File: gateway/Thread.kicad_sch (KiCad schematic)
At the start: 27 parts, among them IC1004 MIC5317-3.3xM5, IC1501 TXB0104PWR, M1501 BT40, Q1501 BSS123, X1501 DEBUG

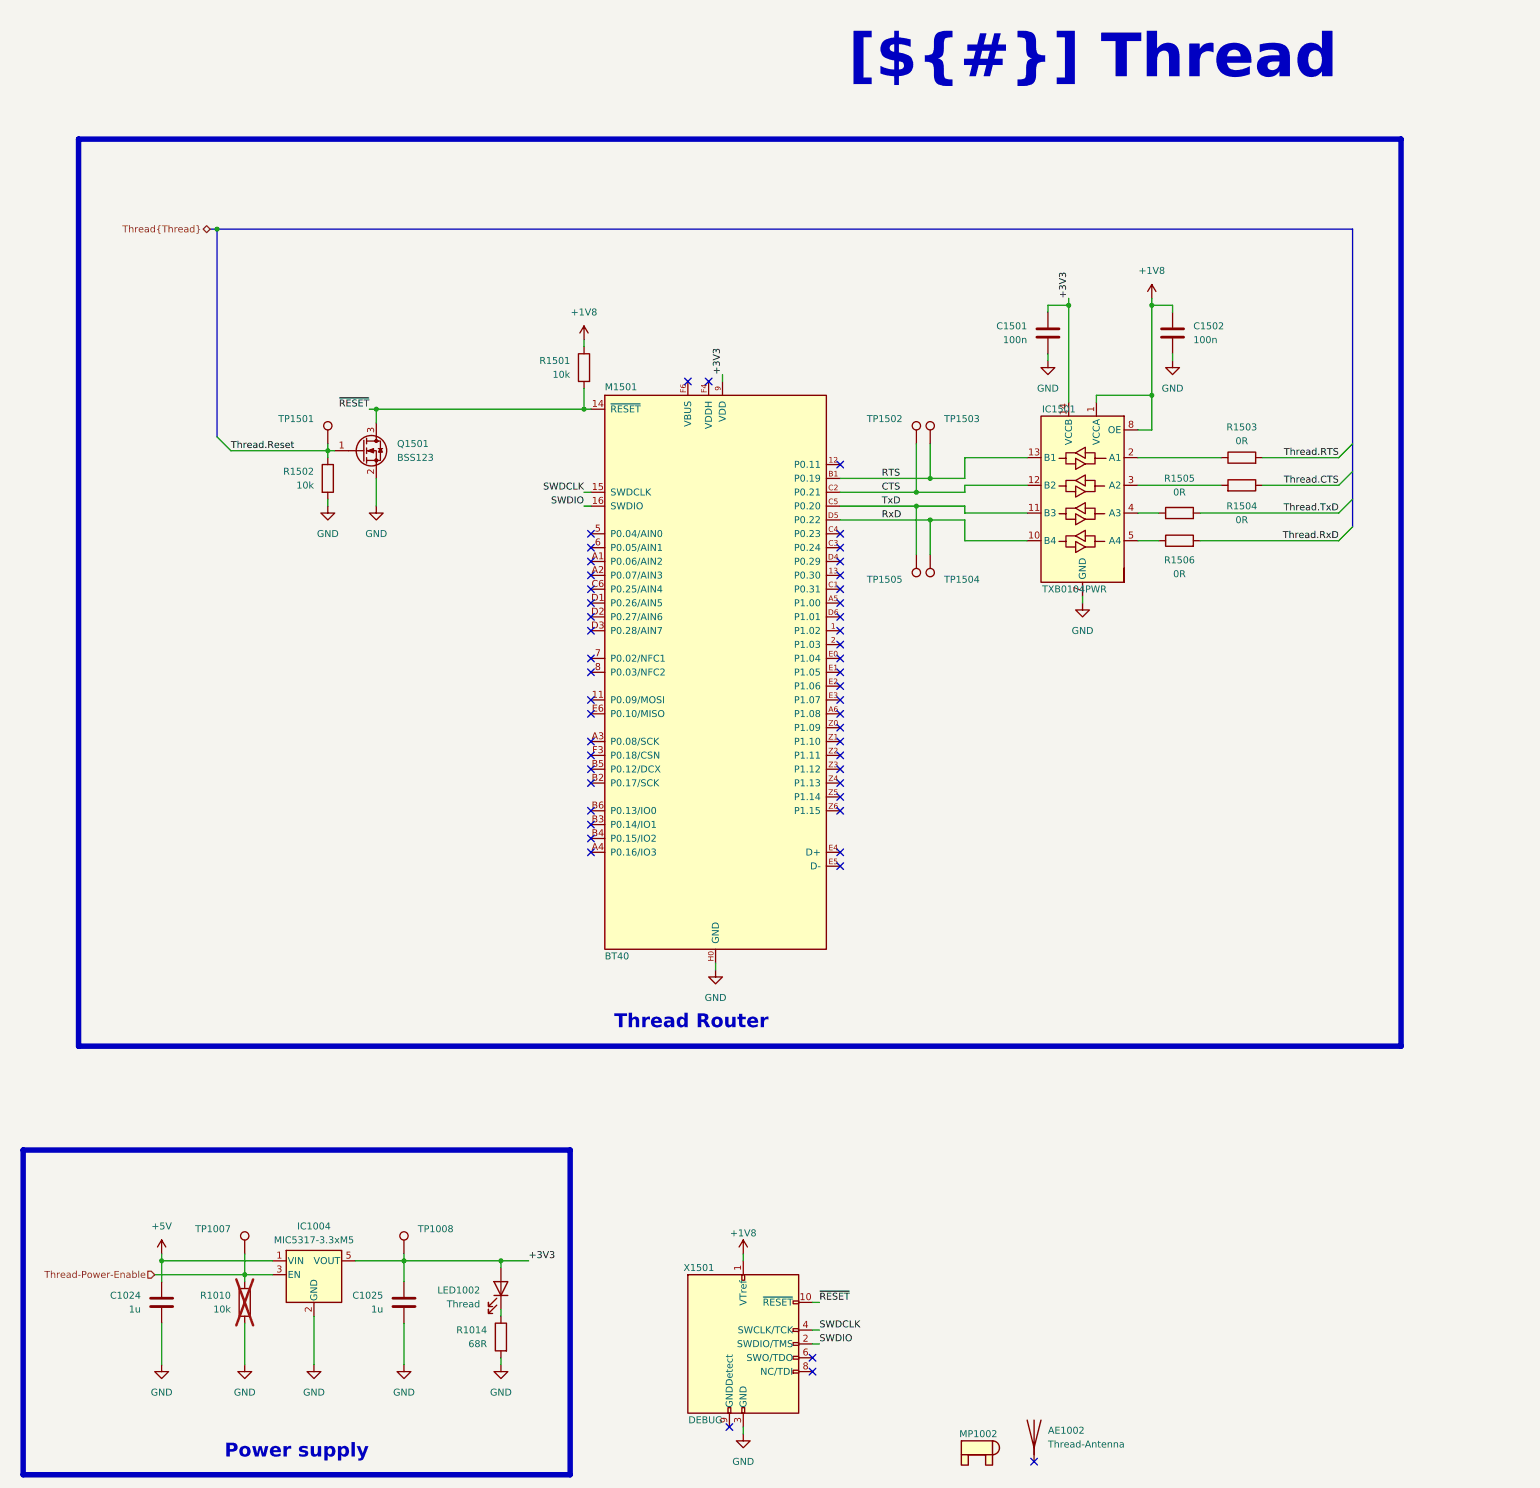
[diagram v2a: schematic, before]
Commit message: Replace level shifter, replace CC2530 with CC2652, fix wrong part numbers
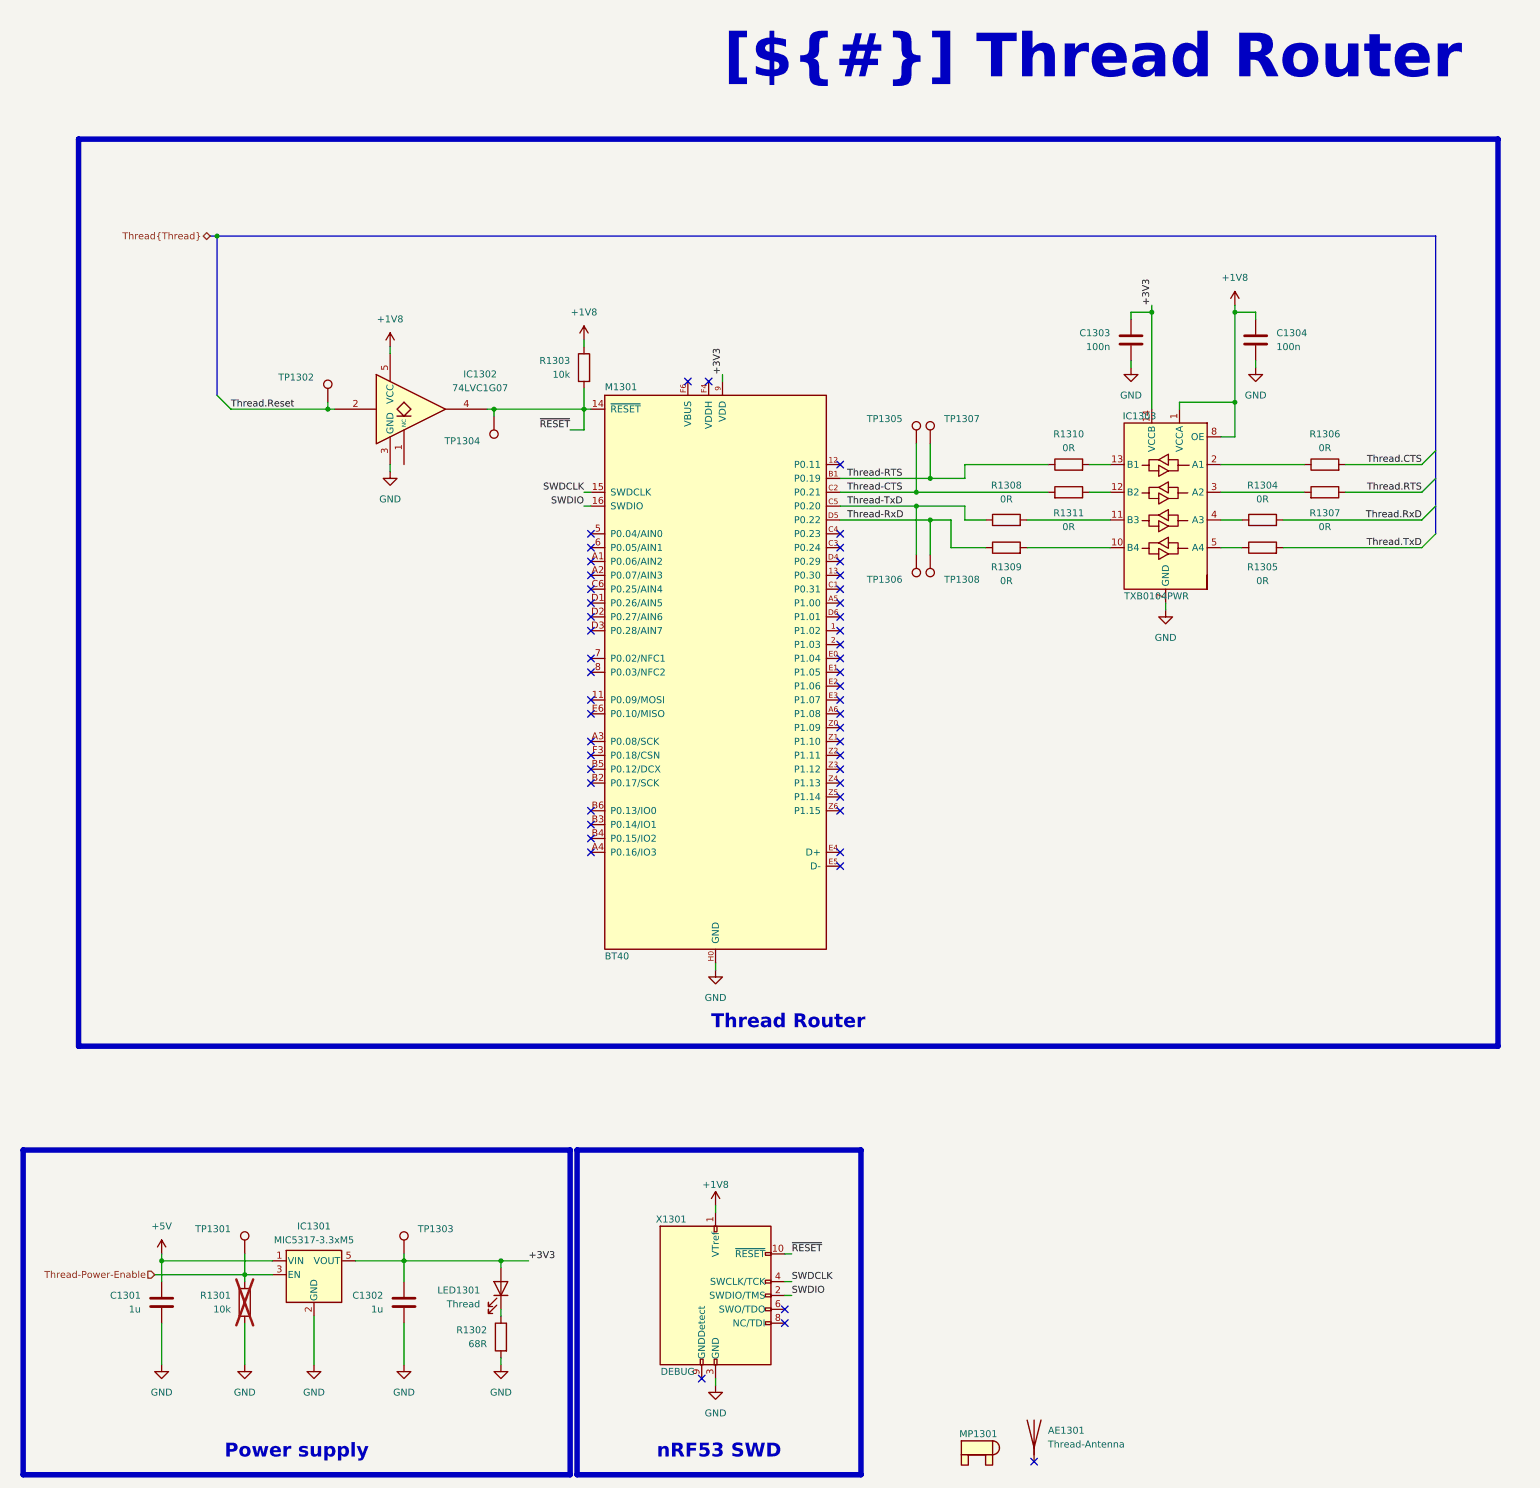
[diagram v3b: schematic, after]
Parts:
- removed Q1501: BSS123, Package_TO_SOT_SMD:SOT-23, symbol Transistor_FET:BSS123
- removed R1502: 10k, Resistor_SMD:R_0805_2012Metric, symbol Device:R
- removed TP1501: ~, Testpoints_Kampi:TestPoint_Pad_1.0x1.0mm, symbol Connector:TestPoint
- added IC1302: 74LVC1G07, Package_TO_SOT_SMD:SOT-353_SC-70-5, symbol 74xGxx:74LVC1G07
- added R1308, R1309, R1310, R1311: 0R, Resistor_SMD:R_0805_2012Metric, symbol Device:R
- added TP1302, TP1304: ~, Testpoints_Kampi:TestPoint_Pad_1.0x1.0mm, symbol Connector:TestPoint
- R1302: renamed from R1014; footprint Resistor_SMD:R_0402_1005Metric -> Resistor_SMD:R_0805_2012Metric
- R1303: renamed from R1501; footprint Resistor_SMD:R_0402_1005Metric -> Resistor_SMD:R_0805_2012Metric; manf# CR0402-JW-103GLF -> CR0805-JW-103GLF
- renumbered AE1002 to AE1301, C1024 to C1301, C1025 to C1302, C1501 to C1303, C1502 to C1304, IC1004 to IC1301, IC1501 to IC1303, LED1002 to LED1301, M1501 to M1301, MP1002 to MP1301, R1010 to R1301, R1505 to R1304, R1506 to R1305, R1503 to R1306, R1504 to R1307, TP1007 to TP1301, TP1008 to TP1303, TP1502 to TP1305, TP1505 to TP1306, TP1503 to TP1307, TP1504 to TP1308, X1501 to X1301
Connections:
- net +1V8: now also IC1302.5 (VCC)
- net GND: now also IC1302.3 (GND)
- net Thread.CTS: now also R1306.2; no longer R1307.1
- net Thread.RTS: now also R1307.1; no longer R1306.2
- net Thread.Reset: now also IC1302.2, TP1302.1
- net Thread.RxD: now also R1304.2; no longer R1305.2
- net Thread.TxD: now also R1305.2; no longer R1304.2
- net ~{RESET}: now also IC1302.4, TP1304.1
- net CTS renamed Thread-CTS
- net Thread-CTS: now also R1311.2; no longer IC1303.12 (B2)
- net RTS renamed Thread-RTS
- net Thread-RTS: now also R1310.1; no longer IC1303.13 (B1)
- net RxD renamed Thread-RxD
- net Thread-RxD: now also R1309.1; no longer IC1303.10 (B4)
- net TxD renamed Thread-TxD
- net Thread-TxD: now also R1308.1; no longer IC1303.11 (B3)
- new net: IC1303.13 (B1), R1310.2
- new net: IC1303.10 (B4), R1309.2
- new net: IC1303.11 (B3), R1308.2
- new net: IC1303.12 (B2), R1311.1
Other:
- title: Thread -> Thread Router
- moved on the sheet: C1303, C1304, IC1303, R1304, R1305, R1306, R1307, X1301
